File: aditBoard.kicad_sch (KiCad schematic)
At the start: 30 parts, among them J1 USB_C_Receptacle_USB2.0, J2 Hashboard0, U2 W25Q16JVUXIQ, U3 RP2040, U4 AP2112K-3.3TRG1, Y1 12MHz

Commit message: bumped version to 2. added RGB LED
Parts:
- added U1: SK6812, aditBoard:LED-SMD_4P-L4.0-W1.6-L, symbol athvfd:SK6812SIDE-A-RVS
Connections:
- net 5V: now also U1.2 (VDD)
- net GND: now also U1.4 (GND)
- net at U3.3 (GPIO1): now also U1.1 (DIN)
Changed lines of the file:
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@@
 	(title_block
 		(title "aditBoard")
-		(date "2024-03-26")
-		(rev "1")
+		(date "2025-06-10")
+		(rev "2")
 	)
 	(text "RP2040 3V3 LDO"
@@
 	)
 	(no_connect
-		(at 176.53 68.58)
-	)
-	(no_connect
 		(at 176.53 129.54)
 	)
@@
 	)
 	(no_connect
+		(at 214.63 71.12)
+	)
+	(no_connect
 		(at 176.53 76.2)
 	)
@@
 	(wire
 		(pts
+			(xy 196.85 71.12) (xy 199.39 71.12)
+		)
+		(stroke
+			(width 0)
+			(type default)
+		)
+	)
+	(wire
+		(pts
 			(xy 139.7 43.18) (xy 139.7 44.45)
 		)
@@
 	(wire
 		(pts
+			(xy 176.53 68.58) (xy 199.39 68.58)
+		)
+		(stroke
+			(width 0)
+			(type default)
+		)
+	)
+	(wire
+		(pts
 			(xy 213.36 138.43) (xy 222.25 138.43)
 		)
@@
 	(wire
 		(pts
+			(xy 214.63 68.58) (xy 218.44 68.58)
+		)
+		(stroke
+			(width 0)
+			(type default)
+		)
+	)
+	(wire
+		(pts
 			(xy 72.39 130.81) (xy 77.47 130.81)
 		)
@@
 		)
 	)
+	(label "GND"
+		(at 218.44 68.58 180)
+		(effects
+			(font
+				(size 1.27 1.27)
+			)
+			(justify right bottom)
+		)
+	)
 	(label "USB_DP"
 		(at 34.29 90.17 0)
@@
 		)
 	)
+	(label "5V"
+		(at 196.85 71.12 0)
+		(effects
+			(font
+				(size 1.27 1.27)
+			)
+			(justify left bottom)
+		)
+	)
 	(label "3V3"
 		(at 69.85 33.02 0)
@@
 					(unit 1)
 				)
+			)
+		)
+	)
+	(symbol
+		(lib_id "athvfd:SK6812SIDE-A-RVS")
+		(at 207.01 69.85 0)
+		(unit 1)
+		(exclude_from_sim no)
+		(in_bom yes)
+		(on_board yes)
+		(dnp no)
+		(property "Reference" "U1"
+			(at 203.2 66.04 0)
+			(effects
+				(font
+					(size 1.27 1.27)
+				)
+			)
+		)
+		(property "Value" "SK6812"
+			(at 208.788 73.66 0)
+			(effects
+				(font
+					(size 1.27 1.27)
+				)
+			)
+		)
+		(property "Footprint" "aditBoard:LED-SMD_4P-L4.0-W1.6-L"
+			(at 216.916 80.772 0)
+			(effects
+				(font
+					(size 1.27 1.27)
+				)
+				(hide yes)
+			)
+		)
+		(property "Datasheet" "https://datasheet.lcsc.com/lcsc/2108251530_OPSCO-Optoelectronics-SK6812SIDE-A-RVS_C2890037.pdf"
+			(at 205.232 78.486 0)
+			(effects
+				(font
+					(size 1.27 1.27)
+				)
+				(hide yes)
+			)
+		)
+		(property "Description" ""
+			(at 199.39 68.58 0)
+			(effects
+				(font
+					(size 1.27 1.27)
+				)
+				(hide yes)
+			)
+		)
+		(property "LCSC" "C2890037"
+			(at 215.138 82.804 0)
+			(effects
+				(font
+					(size 1.27 1.27)
+				)
+				(hide yes)
+			)
+		)
+		(pin "4"
+		)
+		(pin "2"
+		)
+		(pin "1"
+		)
+		(pin "3"
+		)
+		(instances
+			(project "aditBoard"
+				(path "/0c5a2978-3f7a-4586-9b29-75f4eaf2eb2d"
+					(reference "U1")
+					(unit 1)
+				)

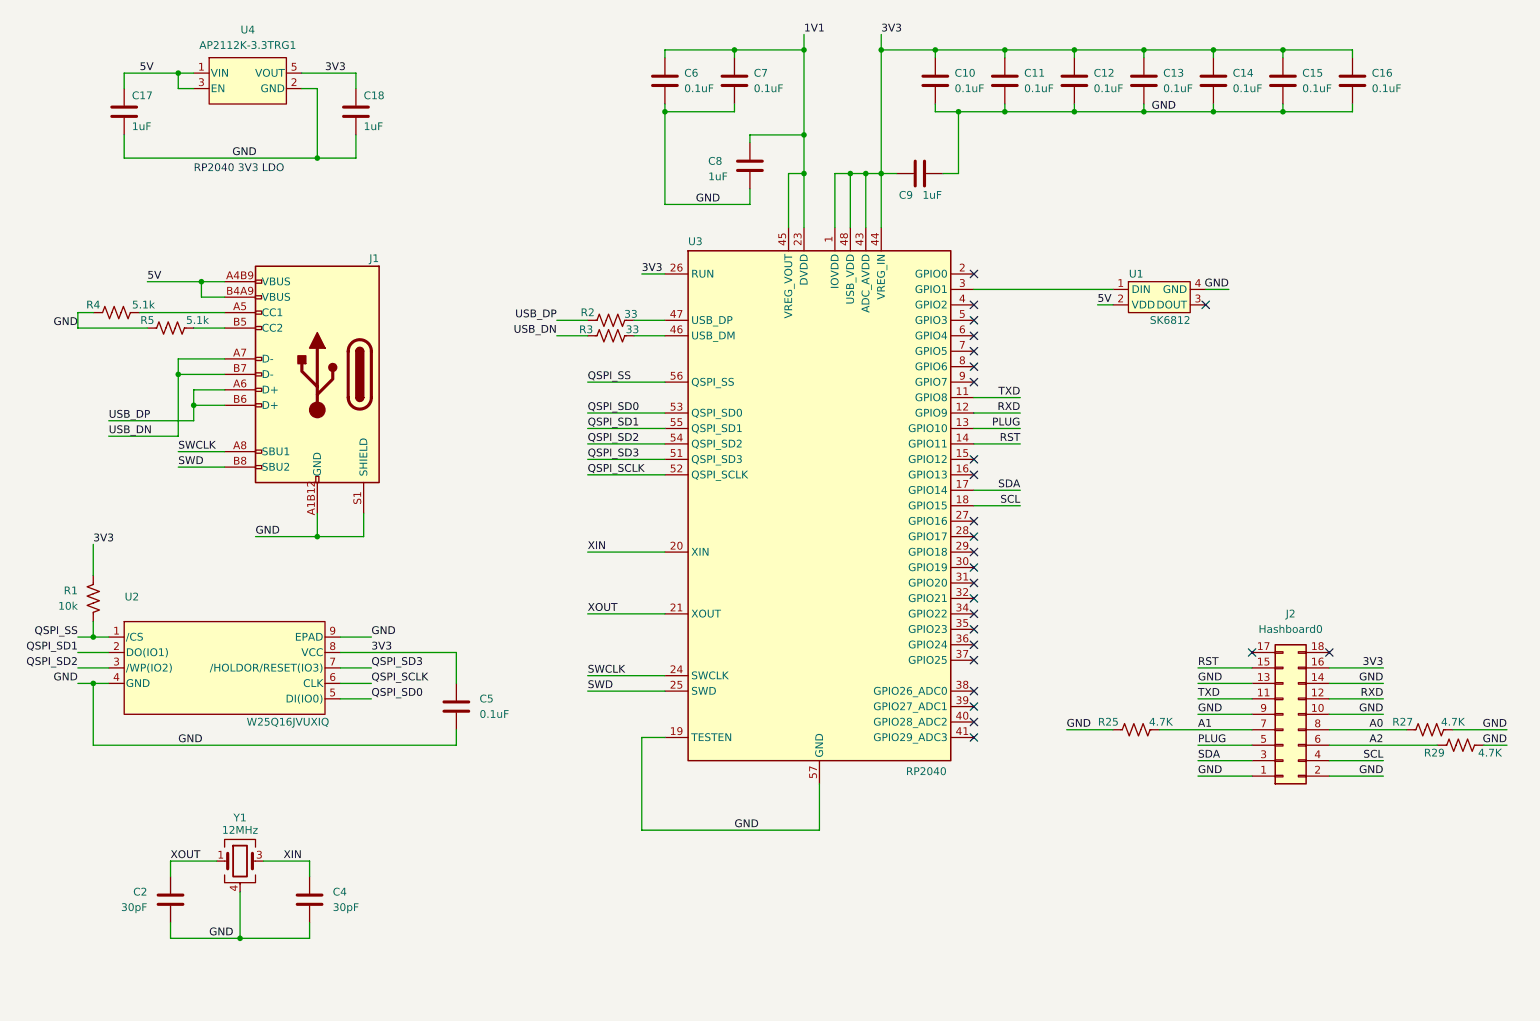
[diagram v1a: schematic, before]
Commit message: Added option for BOOT and RESET buttons. added gerbers and BOM
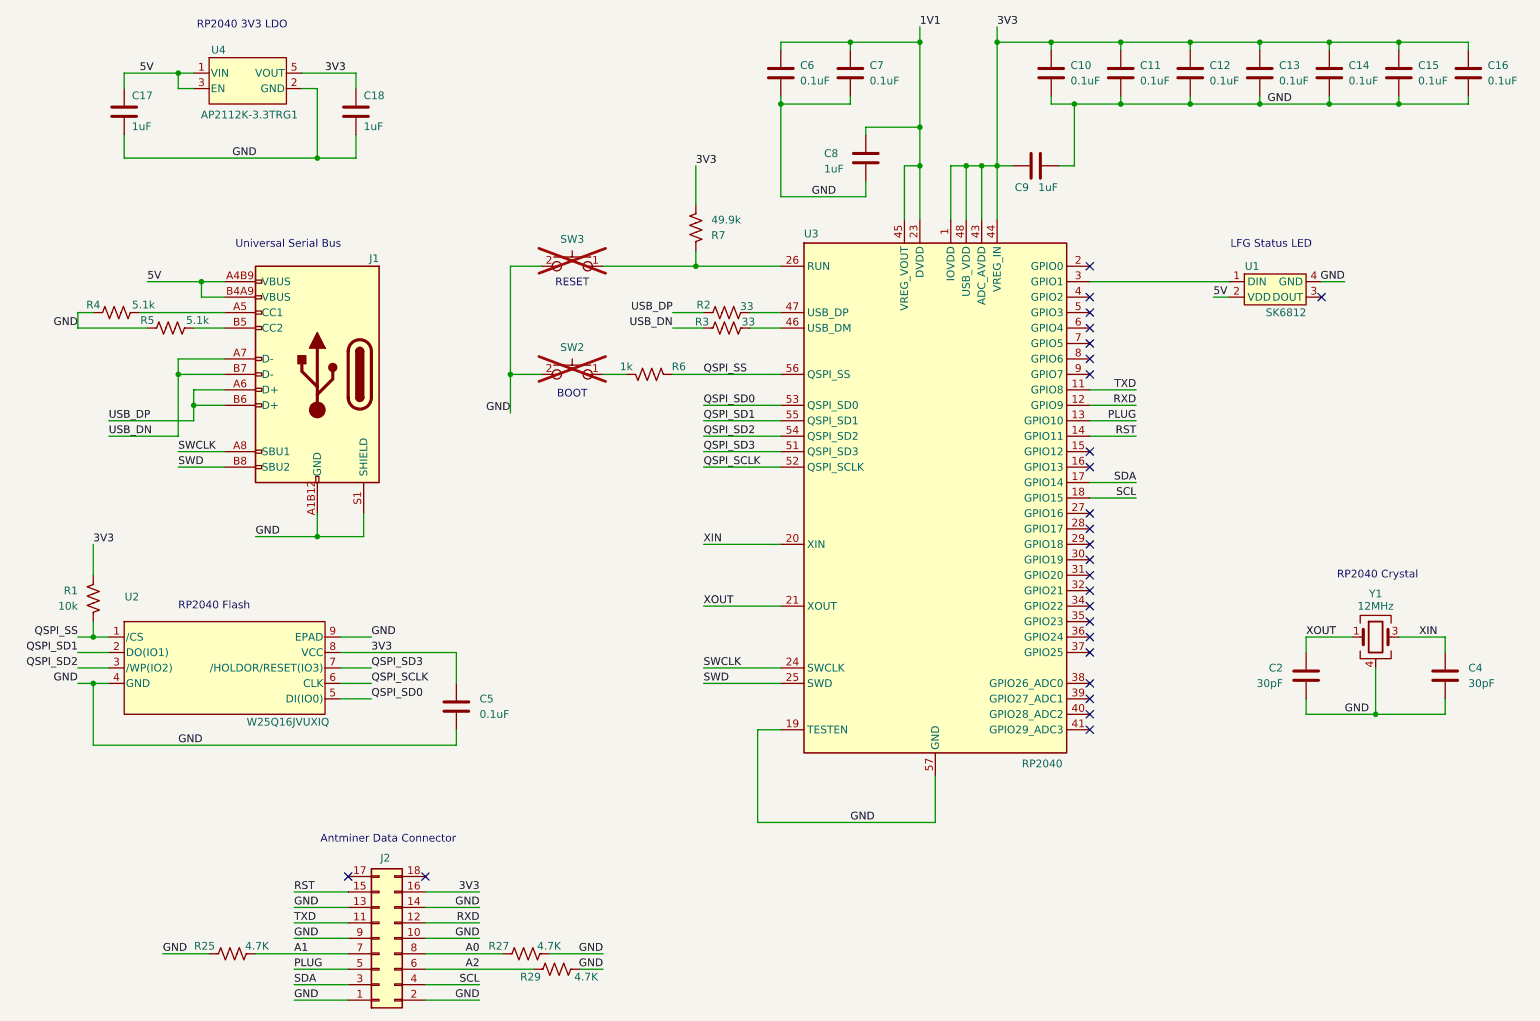
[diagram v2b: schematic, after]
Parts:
- added R6: 1k, Resistor_SMD:R_0402_1005Metric, symbol Device:R_US
- added R7: 49.9k, Resistor_SMD:R_0402_1005Metric, symbol Device:R_US
- added SW2, SW3: GT-TC029B-H025-L1N, aditBoard:SW_CS1213AGF260_CRS, symbol bitaxe:GT-TC029B-H025-L1N
- C10, C11, C12, C13, C14, C15, C16, C5, C6, C7: LCSC (none) -> C307331; LCSC Part C307331 -> (none)
- C17, C18: LCSC (none) -> C52923; LCSC Part C52923 -> (none); PARTNO EMK105BJ105MV-F -> CL05A105KA5NQNC
- C2, C4: LCSC (none) -> C1570; LCSC Part C1570 -> (none)
- C8, C9: LCSC (none) -> C52923; LCSC Part C52923 -> (none)
- J1: LCSC (none) -> C2988369; LCSC Part C2988369 -> (none)
- J2: LCSC (none) -> C3012192; LCSC Part C3012192 -> (none)
- R1: LCSC (none) -> C25744; LCSC Part C25744 -> (none)
- R2, R3: LCSC (none) -> C25105; LCSC Part C25105 -> (none)
- R25, R27, R29: LCSC (none) -> C25900; LCSC Part C25900 -> (none)
- R4, R5: LCSC (none) -> C25905; LCSC Part C25905 -> (none)
- U1: PARTNO (none) -> SK6812SIDE-A-RVS
- U3: LCSC (none) -> C2040; LCSC Part C2040 -> (none)
- U4: LCSC (none) -> C51118; LCSC Part C51118 -> (none)
- Y1: LCSC (none) -> C9002; LCSC Part C9002 -> (none)
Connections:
- net 3V3: now also R7.2; no longer U3.26 (RUN)
- net GND: now also SW2.2, SW3.2
- net QSPI_SS: now also R6.1
- new net: R7.1, SW3.1, U3.26 (RUN)
- new net: R6.2, SW2.1
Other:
- note added: "Antminer Data Connector"
- note added: "BOOT"
- note added: "LFG Status LED"
- note added: "RESET"
- note added: "RP2040 Crystal"
- note added: "RP2040 Flash"
- note added: "Universal Serial Bus"
- moved on the sheet: C10, C11, C12, C13, C14, C15, C16, C2, C4, C6, C7, C8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
